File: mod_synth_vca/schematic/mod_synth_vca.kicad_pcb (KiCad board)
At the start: 2 copper layers, 62.2 x 109.2 mm, 46 parts, among them J1 Conn_02x08_Odd_Even, J2 AudioJack2, J3 AudioJack2, J4 AudioJack2, J5 AudioJack2, J6 AudioJack2, J7 AudioJack2, J8 Conn_01x10_Female, J9 Conn_01x10_Male, U1 TL074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

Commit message: Modify pcb layout
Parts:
- moved R4 64.4 mm to (106.0, 132.7), turned to 90 degrees
- moved R8 64.3 mm to (89.5, 132.7), turned to 90 degrees
- moved R15 52.4 mm to (110.5, 132.7), turned to 90 degrees
- moved R16 51.4 mm to (85.1, 132.7), turned to 90 degrees
- moved D1 24.1 mm to (109.2, 70.5), turned to 90 degrees
- moved D2 22.9 mm to (86.4, 70.5), turned to 90 degrees
- moved U1 19.7 mm to (94.0, 83.2)
- moved C3 12.5 mm to (110.5, 118.1), turned to 90 degrees
- moved C4 11.0 mm to (85.1, 118.1), turned to 90 degrees
- moved R6 10.8 mm to (111.1, 44.5), turned to 90 degrees
- moved R13 10.2 mm to (110.5, 78.7), turned to 270 degrees
- moved R11 8.54 mm to (106.7, 78.7), turned to 270 degrees
- moved R12 5.71 mm to (85.1, 78.7), turned to 270 degrees
- moved R14 4.02 mm to (88.9, 78.7), turned to 270 degrees
- moved D3 3.86 mm to (105.4, 62.9), turned to 270 degrees
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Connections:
- J8 pad 2: /PCB_B_CV_A1 -> /PCB_B_OUT_B
- J8 pad 4: /PCB_B_VOL_A -> /PCB_B_VOL_B
- J8 pad 5: /PCB_B_VOL_B -> /PCB_B_IN_B
- J8 pad 6: /PCB_B_OUT_A -> /PCB_B_IN_A
- J8 pad 7: /PCB_B_OUT_B -> /PCB_B_VOL_A
- J8 pad 8: Net-(J8-Pad8) -> /PCB_B_CV_A1
- J8 pad 9: Net-(J8-Pad9) -> /PCB_B_OUT_A
- J9 pad 2: /PCB_A_CV_A1 -> /PCB_A_OUT_B
- J9 pad 4: /PCB_A_VOL_A -> /PCB_A_VOL_B
- J9 pad 5: /PCB_A_VOL_B -> /PCB_A_IN_B
- J9 pad 6: /PCB_A_OUT_A -> /PCB_A_IN_A
- J9 pad 7: /PCB_A_OUT_B -> /PCB_A_VOL_A
- J9 pad 8: Net-(J9-Pad8) -> /PCB_A_CV_A1
- J9 pad 9: Net-(J9-Pad9) -> /PCB_A_OUT_A
- R11 pad 1: Net-(R11-Pad1) -> /PCB_B_IN_B
- R12 pad 1: Net-(R12-Pad1) -> /PCB_B_IN_A
- R5 pad 1: Net-(R11-Pad1) -> /PCB_A_IN_B
- R9 pad 1: Net-(R12-Pad1) -> /PCB_A_IN_A
- U2 pad 2: Net-(R11-Pad1) -> /PCB_B_IN_B
- U3 pad 2: Net-(R12-Pad1) -> /PCB_B_IN_A
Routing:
- net /PCB_A_+12: track 72.3 -> 0.00 mm
- net Net-(D2-Pad2): track 67.0 -> 0.00 mm
- net /PCB_B_CV_A1: track 64.9 -> 0.00 mm
- net Net-(J4-PadT): track 58.3 -> 0.00 mm
- net Net-(J2-PadT): track 58.3 -> 0.00 mm
- net Net-(R13-Pad1): track 36.1 -> 0.00 mm
- net Net-(R10-Pad1): track 36.1 -> 0.00 mm
- net /PCB_B_OUT_A: track 34.9 -> 0.00 mm
- net Net-(C3-Pad2): track 33.4 -> 0.00 mm
- net +12V: track 29.6 -> 0.00 mm
- net /PCB_B_CV_B1: track 29.3 -> 0.00 mm
- net Net-(C2-Pad1): track 28.6 -> 0.00 mm
- net Net-(C4-Pad2): track 28.5 -> 0.00 mm
- net Net-(R12-Pad1): track 18.8 -> 0.00 mm
- net Net-(R11-Pad1): track 18.8 -> 0.00 mm
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- removed copper zone on B.Cu, net /PCB_A_GND

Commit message: Layout PCB for VCA
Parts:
- moved D2 23.7 mm to (92.7, 47.6), turned to 180 degrees
- moved R11 16.3 mm to (102.9, 62.9)
- moved R13 16.2 mm to (107.3, 62.9)
- moved D3 16.1 mm to (110.5, 47.6), turned to 180 degrees
- moved R14 15.9 mm to (89.5, 62.9)
- moved R12 15.9 mm to (85.1, 62.9)
- moved D1 15.4 mm to (99.7, 58.4)
- moved D4 13.4 mm to (95.9, 50.8)
- moved U1 12.1 mm to (94.0, 95.2)
- moved R4 10.2 mm to (105.4, 122.6), turned to 270 degrees
- moved R8 10.2 mm to (90.2, 122.6), turned to 270 degrees
- moved R18 10.2 mm to (63.5, 121.9), turned to 180 degrees
- moved R6 8.25 mm to (102.9, 44.5)
- moved RV4 3.17 mm to (106.0, 40.6)
- moved R10 0.64 mm to (85.1, 44.5)
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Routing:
- net +12V: track 0.00 -> 161.6 mm
- net -12V: track 0.00 -> 120.5 mm
- net /PCB_A_CV_B1: track 0.00 -> 111.8 mm
- net /PCB_B_CV_B1: track 0.00 -> 98.3 mm
- net /PCB_B_CV_A1: track 0.00 -> 97.7 mm
- net Net-(C4-Pad2): track 0.00 -> 94.8 mm
- net /PCB_A_CV_A1: track 0.00 -> 93.3 mm
- net /PCB_B_IN_A: track 0.00 -> 89.7 mm
- net /PCB_B_IN_B: track 0.00 -> 86.7 mm
- net /PCB_A_IN_B: track 0.00 -> 82.2 mm
- net /PCB_A_IN_A: track 0.00 -> 78.5 mm
- net Net-(C3-Pad2): track 0.00 -> 78.2 mm
- net /PCB_A_+12: track 0.00 -> 74.6 mm
- net /PCB_B_OUT_A: track 0.00 -> 66.5 mm
- net Net-(J4-PadT): track 0.00 -> 59.9 mm
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- added copper zone on B.Cu, net /PCB_A_GND
- added copper zone on F.Cu, net /PCB_A_GND
- added copper zone on B.Cu, net GND
- added copper zone on F.Cu, net GND

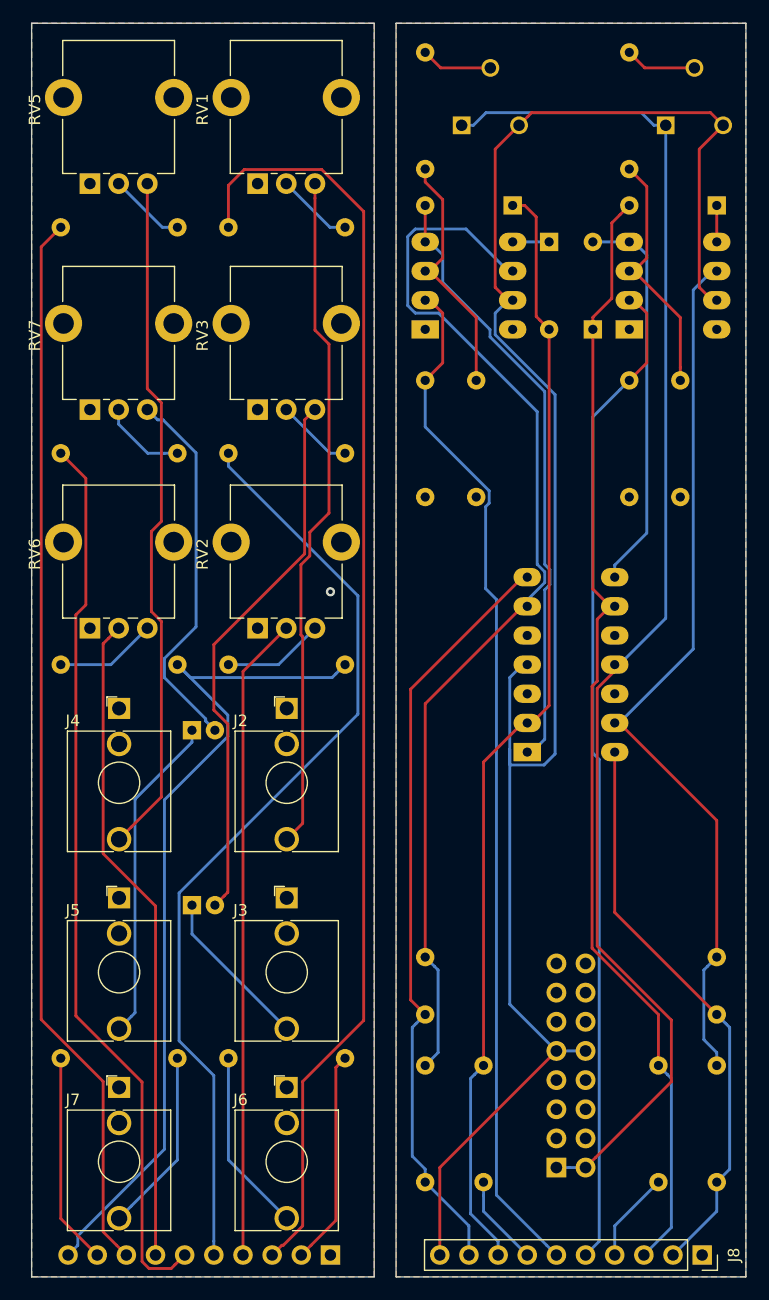
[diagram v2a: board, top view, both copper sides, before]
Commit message: Add support for top of PCB, add folder for kick
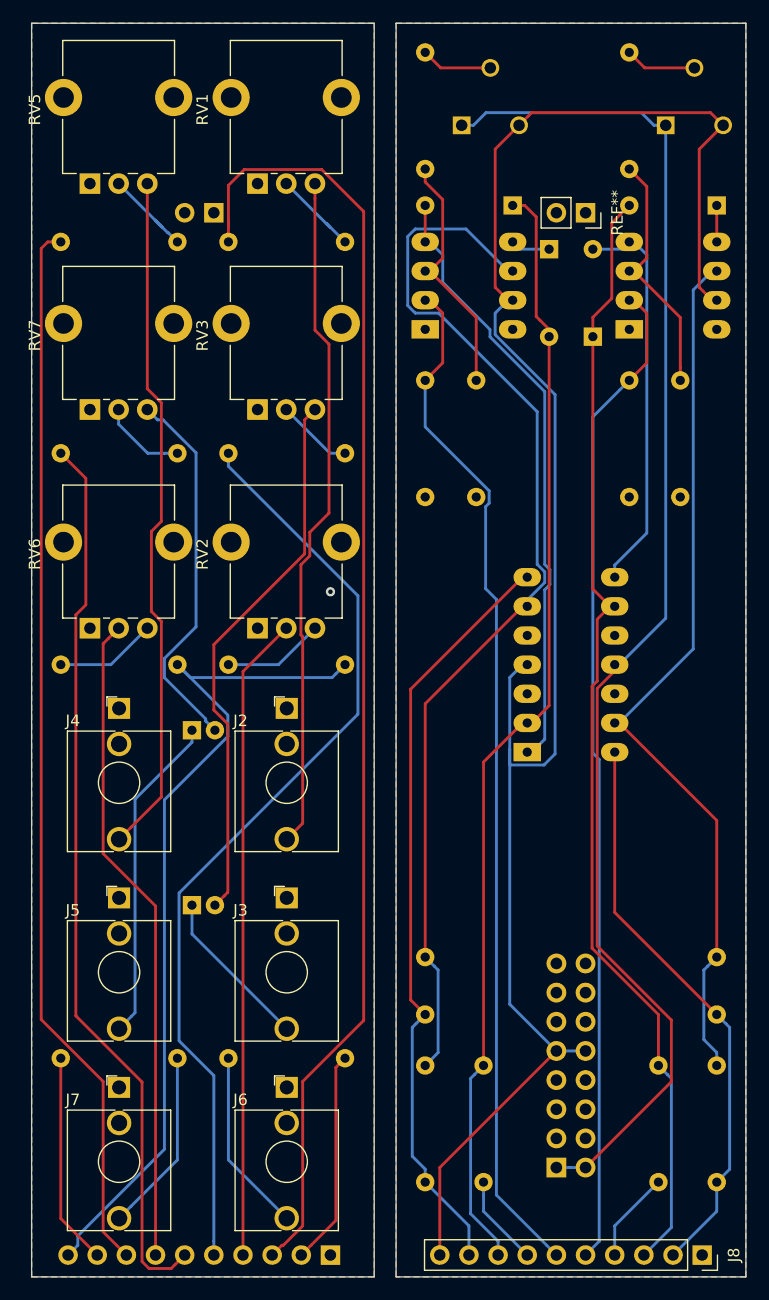
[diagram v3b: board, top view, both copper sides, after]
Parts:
- added REF**: PinSocket_1x02_P2.54mm_Vertical, Connector_PinSocket_2.54mm:PinSocket_1x02_P2.54mm_Vertical, F.Cu at (99.1, 48.3)
- added REF**: PinHeader_1x02_P2.54mm_Vertical, Connector_PinHeader_2.54mm:PinHeader_1x02_P2.54mm_Vertical, B.Cu at (66.7, 48.3)
- moved R3 1.27 mm to (67.9, 50.8)
- moved R7 1.27 mm to (53.3, 50.8)
- moved D4 0.64 mm to (95.9, 51.4)
- moved D1 0.63 mm to (99.7, 59.1)
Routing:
- net /PCB_A_CV_B1: track 111.8 -> 113.7 mm
- net Net-(R7-Pad2): track 6.70 -> 8.09 mm
- net Net-(R3-Pad2): track 6.70 -> 7.64 mm
- net /PCB_A_CV_A1: track 93.3 -> 92.7 mm

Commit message: Volume resistor should be 20k
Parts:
- removed REF**: PinSocket_1x02_P2.54mm_Vertical, Connector_PinSocket_2.54mm:PinSocket_1x02_P2.54mm_Vertical
- removed REF**: PinHeader_1x02_P2.54mm_Vertical, Connector_PinHeader_2.54mm:PinHeader_1x02_P2.54mm_Vertical
- R1, R2: value 10k -> 20k
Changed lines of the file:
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@@
     (tracks 332)
     (zones 0)
-    (modules 48)
+    (modules 46)
     (nets 56)
   )
@@
     (add_net "Net-(U3-Pad8)")
   )
-  (module Connector_PinSocket_2.54mm:PinSocket_1x02_P2.54mm_Vertical (layer F.Cu)
-    (at 99.06 48.26 270)
-    (descr "Through hole straight socket strip, 1x02, 2.54mm pitch, single row (from Kicad 4.0.7), script generated")
-    (tags "Through hole socket strip THT 1x02 2.54mm single row")
-    (fp_text reference REF** (at 0 -2.77 90) (layer F.SilkS)
-      (effects (font (size 1 1) (thickness 0.15)))
-    )
-    (fp_text value PinSocket_1x02_P2.54mm_Vertical (at 0 5.31 90) (layer F.Fab)
-      (effects (font (size 1 1) (thickness 0.15)))
-    )
-    (fp_text user %R (at 0 1.27) (layer F.Fab)
-      (effects (font (size 1 1) (thickness 0.15)))
-    )
-    (fp_line (start -1.8 4.3) (end -1.8 -1.8) (layer F.CrtYd) (width 0.05))
-    (fp_line (start 1.75 4.3) (end -1.8 4.3) (layer F.CrtYd) (width 0.05))
-    (fp_line (start 1.75 -1.8) (end 1.75 4.3) (layer F.CrtYd) (width 0.05))
-    (fp_line (start -1.8 -1.8) (end 1.75 -1.8) (layer F.CrtYd) (width 0.05))
-    (fp_line (start 0 -1.33) (end 1.33 -1.33) (layer F.SilkS) (width 0.12))
-    (fp_line (start 1.33 -1.33) (end 1.33 0) (layer F.SilkS) (width 0.12))
-    (fp_line (start 1.33 1.27) (end 1.33 3.87) (layer F.SilkS) (width 0.12))
-    (fp_line (start -1.33 3.87) (end 1.33 3.87) (layer F.SilkS) (width 0.12))
-    (fp_line (start -1.33 1.27) (end -1.33 3.87) (layer F.SilkS) (width 0.12))
-    (fp_line (start -1.33 1.27) (end 1.33 1.27) (layer F.SilkS) (width 0.12))
-    (fp_line (start -1.27 3.81) (end -1.27 -1.27) (layer F.Fab) (width 0.1))
-    (fp_line (start 1.27 3.81) (end -1.27 3.81) (layer F.Fab) (width 0.1))
-    (fp_line (start 1.27 -0.635) (end 1.27 3.81) (layer F.Fab) (width 0.1))
-    (fp_line (start 0.635 -1.27) (end 1.27 -0.635) (layer F.Fab) (width 0.1))
-    (fp_line (start -1.27 -1.27) (end 0.635 -1.27) (layer F.Fab) (width 0.1))
-    (pad 2 thru_hole oval (at 0 2.54 270) (size 1.7 1.7) (drill 1) (layers *.Cu *.Mask))
-    (pad 1 thru_hole rect (at 0 0 270) (size 1.7 1.7) (drill 1) (layers *.Cu *.Mask))
-    (model ${KISYS3DMOD}/Connector_PinSocket_2.54mm.3dshapes/PinSocket_1x02_P2.54mm_Vertical.wrl
-      (at (xyz 0 0 0))
-      (scale (xyz 1 1 1))
-      (rotate (xyz 0 0 0))
-    )
-  )
-  (module Connector_PinHeader_2.54mm:PinHeader_1x02_P2.54mm_Vertical (layer B.Cu)
-    (at 66.675 48.26 90)
-    (descr "Through hole straight pin header, 1x02, 2.54mm pitch, single row")
-    (tags "Through hole pin header THT 1x02 2.54mm single row")
-    (fp_text reference REF** (at 0 2.33 90) (layer B.SilkS)
-      (effects (font (size 1 1) (thickness 0.15)) (justify mirror))
-    )
-    (fp_text value PinHeader_1x02_P2.54mm_Vertical (at 0 -4.87 90) (layer B.Fab)
-      (effects (font (size 1 1) (thickness 0.15)) (justify mirror))
-    )
-    (fp_text user %R (at 0 -1.27 180) (layer B.Fab)
-      (effects (font (size 1 1) (thickness 0.15)) (justify mirror))
-    )
-    (fp_line (start 1.8 1.8) (end -1.8 1.8) (layer B.CrtYd) (width 0.05))
-    (fp_line (start 1.8 -4.35) (end 1.8 1.8) (layer B.CrtYd) (width 0.05))
-    (fp_line (start -1.8 -4.35) (end 1.8 -4.35) (layer B.CrtYd) (width 0.05))
-    (fp_line (start -1.8 1.8) (end -1.8 -4.35) (layer B.CrtYd) (width 0.05))
-    (fp_line (start -1.33 1.33) (end 0 1.33) (layer B.SilkS) (width 0.12))
-    (fp_line (start -1.33 0) (end -1.33 1.33) (layer B.SilkS) (width 0.12))
-    (fp_line (start -1.33 -1.27) (end 1.33 -1.27) (layer B.SilkS) (width 0.12))
-    (fp_line (start 1.33 -1.27) (end 1.33 -3.87) (layer B.SilkS) (width 0.12))
-    (fp_line (start -1.33 -1.27) (end -1.33 -3.87) (layer B.SilkS) (width 0.12))
-    (fp_line (start -1.33 -3.87) (end 1.33 -3.87) (layer B.SilkS) (width 0.12))
-    (fp_line (start -1.27 0.635) (end -0.635 1.27) (layer B.Fab) (width 0.1))
-    (fp_line (start -1.27 -3.81) (end -1.27 0.635) (layer B.Fab) (width 0.1))
-    (fp_line (start 1.27 -3.81) (end -1.27 -3.81) (layer B.Fab) (width 0.1))
-    (fp_line (start 1.27 1.27) (end 1.27 -3.81) (layer B.Fab) (width 0.1))
-    (fp_line (start -0.635 1.27) (end 1.27 1.27) (layer B.Fab) (width 0.1))
-    (pad 2 thru_hole oval (at 0 -2.54 90) (size 1.7 1.7) (drill 1) (layers *.Cu *.Mask))
-    (pad 1 thru_hole rect (at 0 0 90) (size 1.7 1.7) (drill 1) (layers *.Cu *.Mask))
-    (model ${KISYS3DMOD}/Connector_PinHeader_2.54mm.3dshapes/PinHeader_1x02_P2.54mm_Vertical.wrl
-      (at (xyz 0 0 0))
-      (scale (xyz 1 1 1))
-      (rotate (xyz 0 0 0))
-    )
-  )
   (module Connector_PinHeader_2.54mm:PinHeader_1x10_P2.54mm_Vertical (layer B.Cu)
     (at 76.835 139.065 90)
@@
       (effects (font (size 1 1) (thickness 0.15)) (justify mirror))
     )
-    (fp_text value 10k (at 5.08 -2.37) (layer B.Fab)
+    (fp_text value 20k (at 5.08 -2.37) (layer B.Fab)
       (effects (font (size 1 1) (thickness 0.15)) (justify mirror))
     )
@@
       (effects (font (size 1 1) (thickness 0.15)) (justify mirror))
     )
-    (fp_text value 10k (at 5.08 -2.37) (layer B.Fab)
-      (effects (font (size 1 1) (thickness 0.15)) (justify mirror))
-    )
+    (fp_text value 20k (at 5.08 -2.37) (layer B.Fab)
+      (effects (font (size 1 1) (thickness 0.15)) (justify mirror))
+    )

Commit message: re-add VCA support pins
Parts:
- added REF**: PinSocket_1x02_P2.54mm_Vertical, Connector_PinSocket_2.54mm:PinSocket_1x02_P2.54mm_Vertical, F.Cu at (99.1, 48.3)
- added REF**: PinHeader_1x02_P2.54mm_Vertical, Connector_PinHeader_2.54mm:PinHeader_1x02_P2.54mm_Vertical, B.Cu at (66.7, 48.3)
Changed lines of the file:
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@@
     (tracks 332)
     (zones 0)
-    (modules 46)
+    (modules 48)
     (nets 56)
   )
@@
     (add_net "Net-(U3-Pad8)")
   )
+  (module Connector_PinSocket_2.54mm:PinSocket_1x02_P2.54mm_Vertical (layer F.Cu)
+    (at 99.06 48.26 270)
+    (descr "Through hole straight socket strip, 1x02, 2.54mm pitch, single row (from Kicad 4.0.7), script generated")
+    (tags "Through hole socket strip THT 1x02 2.54mm single row")
+    (fp_text reference REF** (at 0 -2.77 90) (layer F.SilkS)
+      (effects (font (size 1 1) (thickness 0.15)))
+    )
+    (fp_text value PinSocket_1x02_P2.54mm_Vertical (at 0 5.31 90) (layer F.Fab)
+      (effects (font (size 1 1) (thickness 0.15)))
+    )
+    (fp_text user %R (at 0 1.27) (layer F.Fab)
+      (effects (font (size 1 1) (thickness 0.15)))
+    )
+    (fp_line (start -1.8 4.3) (end -1.8 -1.8) (layer F.CrtYd) (width 0.05))
+    (fp_line (start 1.75 4.3) (end -1.8 4.3) (layer F.CrtYd) (width 0.05))
+    (fp_line (start 1.75 -1.8) (end 1.75 4.3) (layer F.CrtYd) (width 0.05))
+    (fp_line (start -1.8 -1.8) (end 1.75 -1.8) (layer F.CrtYd) (width 0.05))
+    (fp_line (start 0 -1.33) (end 1.33 -1.33) (layer F.SilkS) (width 0.12))
+    (fp_line (start 1.33 -1.33) (end 1.33 0) (layer F.SilkS) (width 0.12))
+    (fp_line (start 1.33 1.27) (end 1.33 3.87) (layer F.SilkS) (width 0.12))
+    (fp_line (start -1.33 3.87) (end 1.33 3.87) (layer F.SilkS) (width 0.12))
+    (fp_line (start -1.33 1.27) (end -1.33 3.87) (layer F.SilkS) (width 0.12))
+    (fp_line (start -1.33 1.27) (end 1.33 1.27) (layer F.SilkS) (width 0.12))
+    (fp_line (start -1.27 3.81) (end -1.27 -1.27) (layer F.Fab) (width 0.1))
+    (fp_line (start 1.27 3.81) (end -1.27 3.81) (layer F.Fab) (width 0.1))
+    (fp_line (start 1.27 -0.635) (end 1.27 3.81) (layer F.Fab) (width 0.1))
+    (fp_line (start 0.635 -1.27) (end 1.27 -0.635) (layer F.Fab) (width 0.1))
+    (fp_line (start -1.27 -1.27) (end 0.635 -1.27) (layer F.Fab) (width 0.1))
+    (pad 2 thru_hole oval (at 0 2.54 270) (size 1.7 1.7) (drill 1) (layers *.Cu *.Mask))
+    (pad 1 thru_hole rect (at 0 0 270) (size 1.7 1.7) (drill 1) (layers *.Cu *.Mask))
+    (model ${KISYS3DMOD}/Connector_PinSocket_2.54mm.3dshapes/PinSocket_1x02_P2.54mm_Vertical.wrl
+      (at (xyz 0 0 0))
+      (scale (xyz 1 1 1))
+      (rotate (xyz 0 0 0))
+    )
+  )
+  (module Connector_PinHeader_2.54mm:PinHeader_1x02_P2.54mm_Vertical (layer B.Cu)
+    (at 66.675 48.26 90)
+    (descr "Through hole straight pin header, 1x02, 2.54mm pitch, single row")
+    (tags "Through hole pin header THT 1x02 2.54mm single row")
+    (fp_text reference REF** (at 0 2.33 90) (layer B.SilkS)
+      (effects (font (size 1 1) (thickness 0.15)) (justify mirror))
+    )
+    (fp_text value PinHeader_1x02_P2.54mm_Vertical (at 0 -4.87 90) (layer B.Fab)
+      (effects (font (size 1 1) (thickness 0.15)) (justify mirror))
+    )
+    (fp_text user %R (at 0 -1.27 180) (layer B.Fab)
+      (effects (font (size 1 1) (thickness 0.15)) (justify mirror))
+    )
+    (fp_line (start 1.8 1.8) (end -1.8 1.8) (layer B.CrtYd) (width 0.05))
+    (fp_line (start 1.8 -4.35) (end 1.8 1.8) (layer B.CrtYd) (width 0.05))
+    (fp_line (start -1.8 -4.35) (end 1.8 -4.35) (layer B.CrtYd) (width 0.05))
+    (fp_line (start -1.8 1.8) (end -1.8 -4.35) (layer B.CrtYd) (width 0.05))
+    (fp_line (start -1.33 1.33) (end 0 1.33) (layer B.SilkS) (width 0.12))
+    (fp_line (start -1.33 0) (end -1.33 1.33) (layer B.SilkS) (width 0.12))
+    (fp_line (start -1.33 -1.27) (end 1.33 -1.27) (layer B.SilkS) (width 0.12))
+    (fp_line (start 1.33 -1.27) (end 1.33 -3.87) (layer B.SilkS) (width 0.12))
+    (fp_line (start -1.33 -1.27) (end -1.33 -3.87) (layer B.SilkS) (width 0.12))
+    (fp_line (start -1.33 -3.87) (end 1.33 -3.87) (layer B.SilkS) (width 0.12))
+    (fp_line (start -1.27 0.635) (end -0.635 1.27) (layer B.Fab) (width 0.1))
+    (fp_line (start -1.27 -3.81) (end -1.27 0.635) (layer B.Fab) (width 0.1))
+    (fp_line (start 1.27 -3.81) (end -1.27 -3.81) (layer B.Fab) (width 0.1))
+    (fp_line (start 1.27 1.27) (end 1.27 -3.81) (layer B.Fab) (width 0.1))
+    (fp_line (start -0.635 1.27) (end 1.27 1.27) (layer B.Fab) (width 0.1))
+    (pad 2 thru_hole oval (at 0 -2.54 90) (size 1.7 1.7) (drill 1) (layers *.Cu *.Mask))
+    (pad 1 thru_hole rect (at 0 0 90) (size 1.7 1.7) (drill 1) (layers *.Cu *.Mask))
+    (model ${KISYS3DMOD}/Connector_PinHeader_2.54mm.3dshapes/PinHeader_1x02_P2.54mm_Vertical.wrl
+      (at (xyz 0 0 0))
+      (scale (xyz 1 1 1))
+      (rotate (xyz 0 0 0))
+    )
+  )
   (module Connector_PinHeader_2.54mm:PinHeader_1x10_P2.54mm_Vertical (layer B.Cu)
